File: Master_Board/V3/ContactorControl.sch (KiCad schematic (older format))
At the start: 29 parts, among them J701 649004227222, J702 649004227222, J703 649004227222, J704 649002227222, Q701 BC849BLT1G, Q702 BC849BLT1G, Q703 BC849BLT1G, Q704 BC849BLT1G, U701 CPC1117NTR

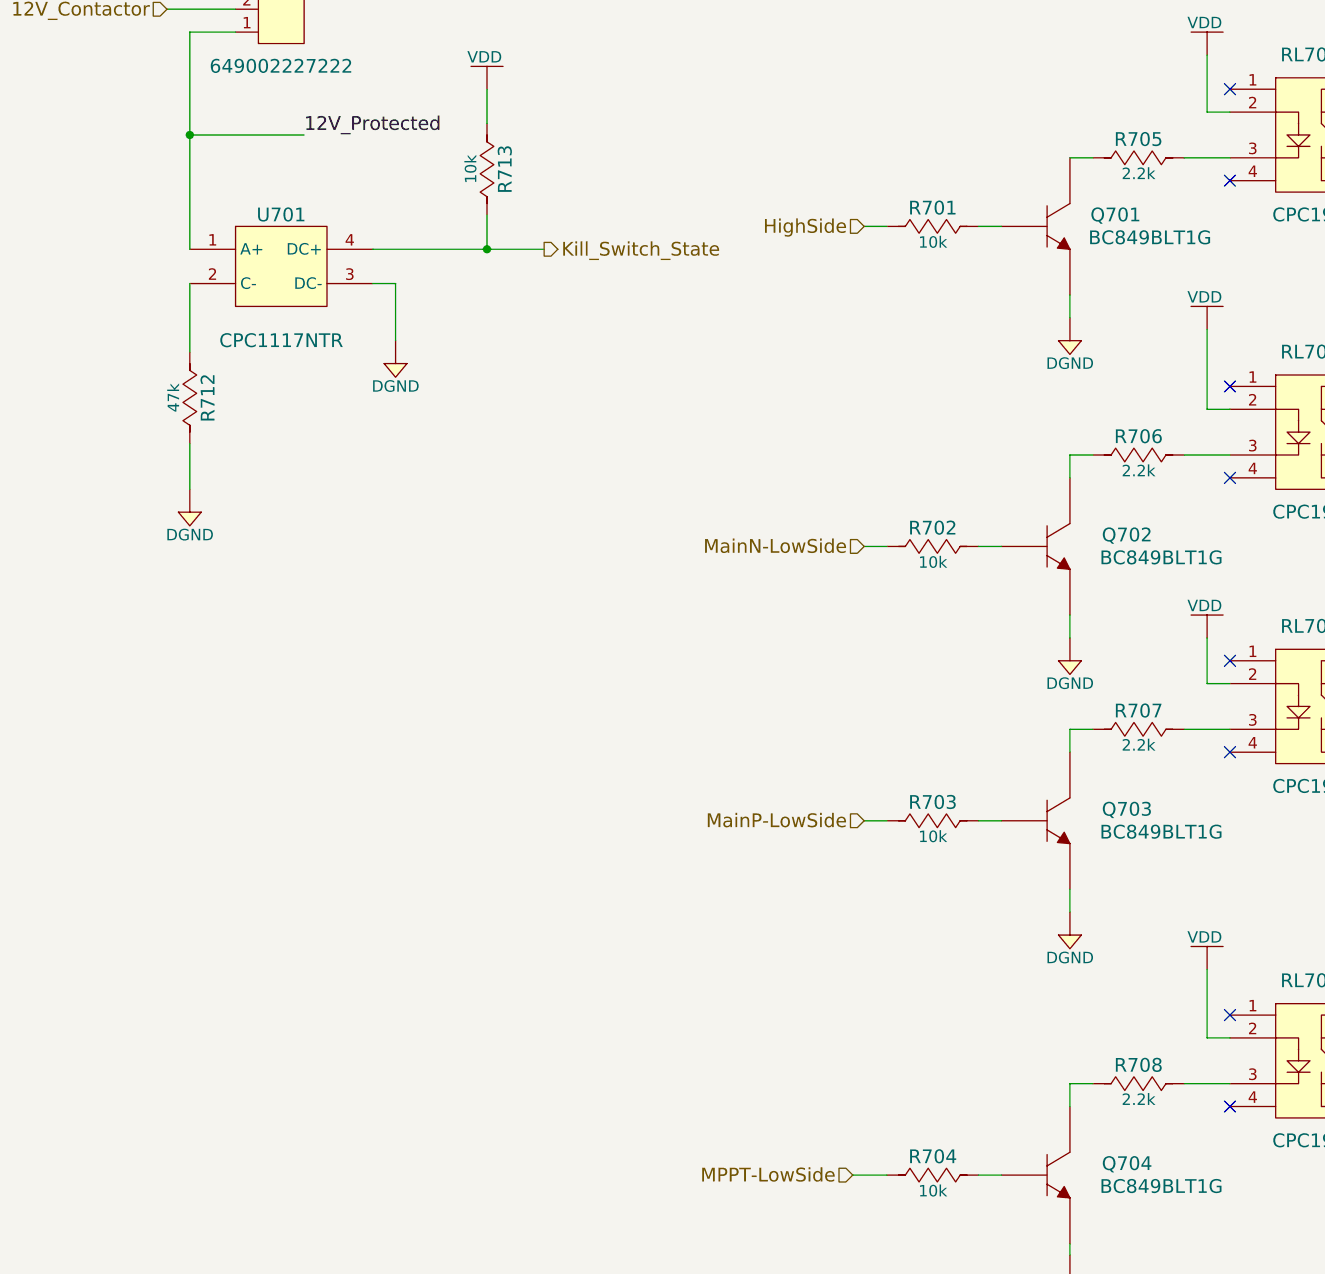
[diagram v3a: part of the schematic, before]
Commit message: Changed values of optocoupler resistor
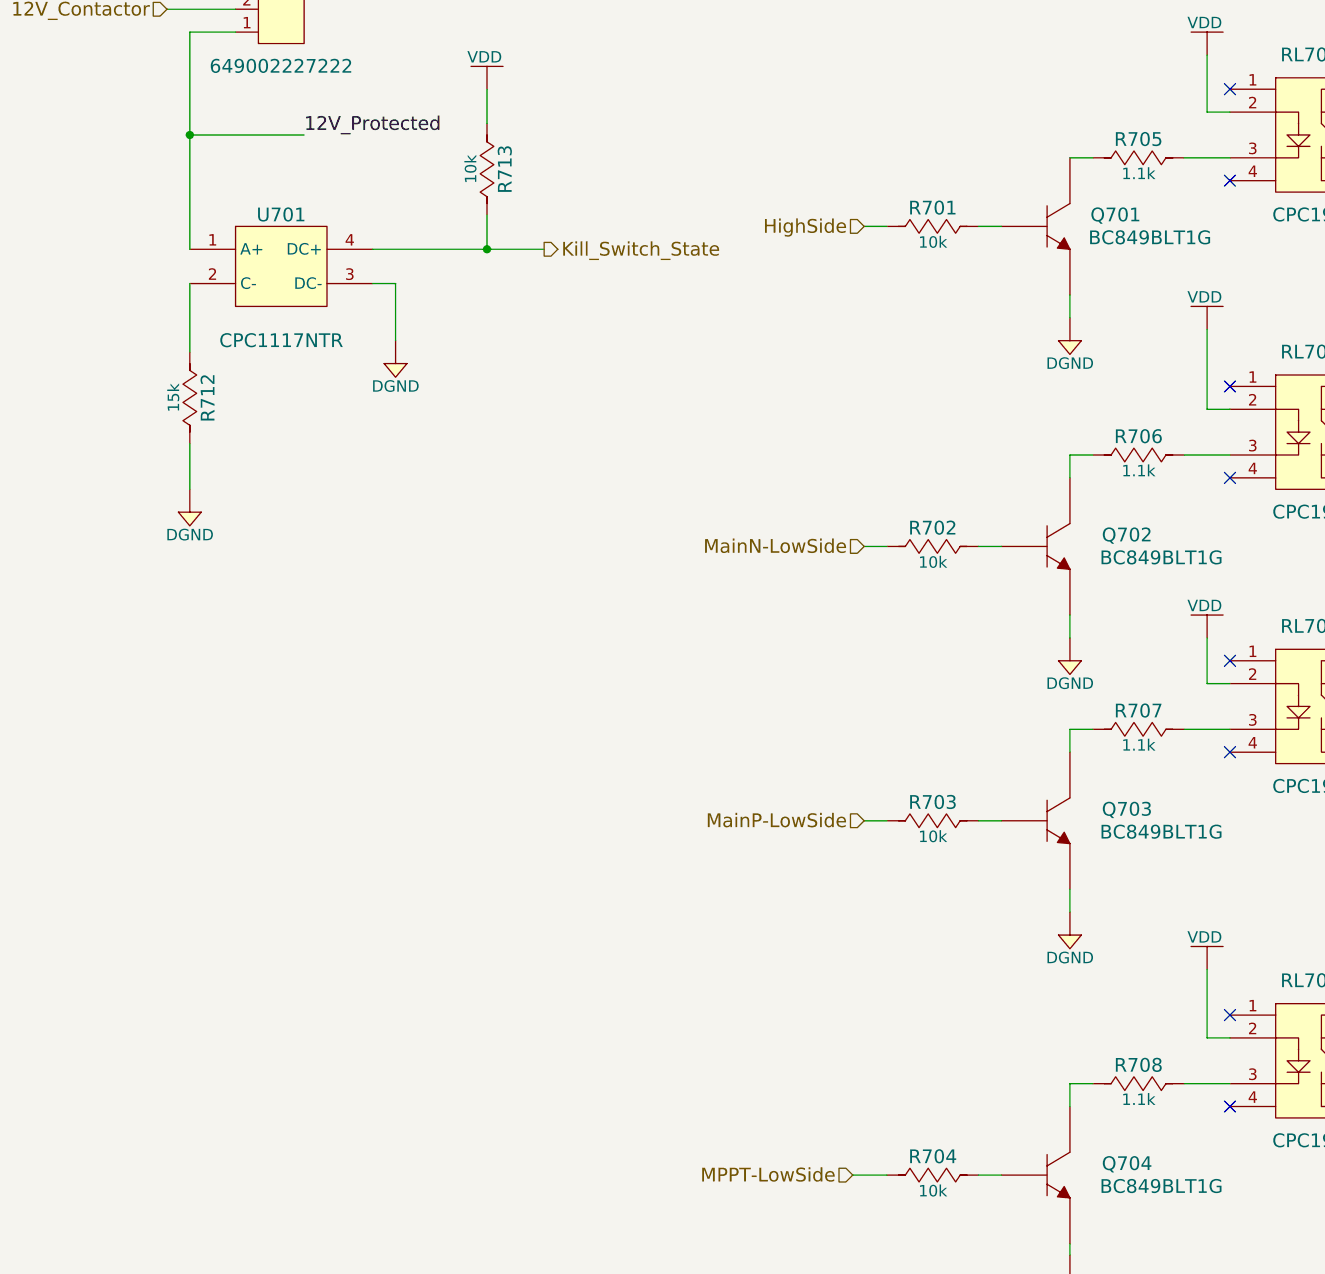
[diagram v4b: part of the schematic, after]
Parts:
- removed R705, R706, R707, R708: RC0805JR-072K2L, Resistors:R0805, symbol RC0805JR-072K2L
- removed R712: RC0805JR-0747KL, Resistors:R0805, symbol RC0805JR-0747KL
- added R705, R706, R707, R708: RC0805FR-071K1L, Resistors:R0805, symbol RC0805FR-071K1L
- added R712: RC0805JR-0715KL, Resistors:R0805, symbol RC0805JR-0715KL
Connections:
- net DGND: now also R712.2
- net at Q701.3 (C): now also R705.1
- net at RL701.3: now also R705.2
- net at RL702.3: now also R706.2
- net at RL703.3: now also R707.2
- net at RL704.3: now also R708.2
- net at Q702.3 (C): now also R706.1
- net at Q703.3 (C): now also R707.1
- net at Q704.3 (C): now also R708.1
- net at U701.2 (C-): now also R712.1
